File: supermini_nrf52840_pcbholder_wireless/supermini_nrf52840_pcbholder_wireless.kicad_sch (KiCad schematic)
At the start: 14 parts, among them J10 Conn_01x08_Pin, J11 Conn_01x08_Pin, J12 Conn_01x08_Pin, J5 Conn_01x02_Pin, J6 Conn_01x02_Pin, J7 Conn_01x04_Pin, J8 Conn_01x04_Pin, J9 Conn_01x08_Pin, SW1 SW_SPDT, SW2 SW_SPST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

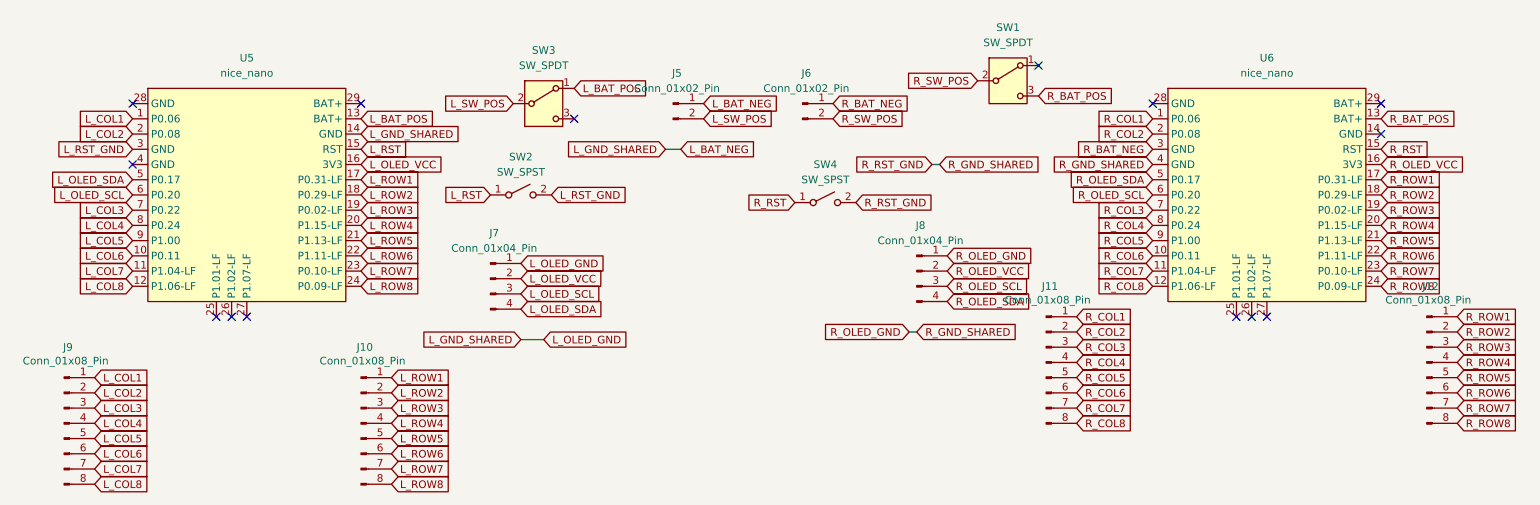
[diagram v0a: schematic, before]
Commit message: change power switch footprint and supermini board placement
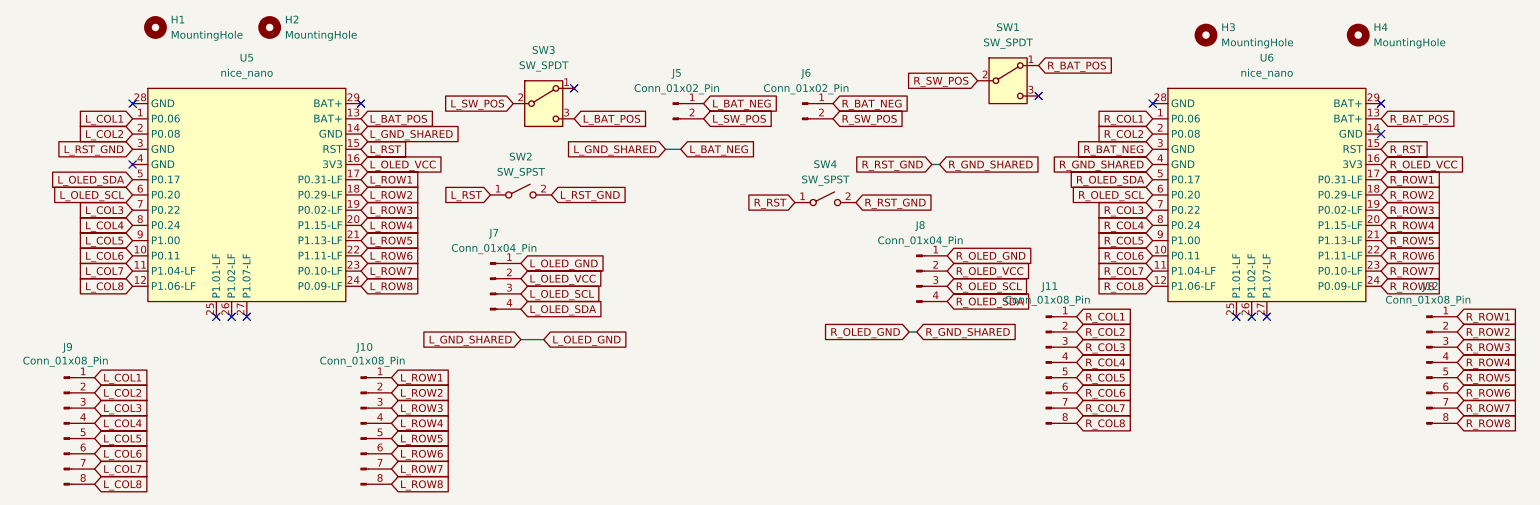
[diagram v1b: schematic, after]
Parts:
- added H1, H2, H3, H4: MountingHole, #footprint:M1.4_tapping_Hole_rev2, symbol Mechanical:MountingHole
- SW1, SW3: footprint #footprint:TGSW_MSK-12D19 -> SLW_864574_5A_RA_N_D:SW_SLW-864574-5A-RA-N-D
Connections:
- net L_BAT_POS: now also SW3.3 (C); no longer SW3.1 (A)
- net R_BAT_POS: now also SW1.1 (A); no longer SW1.3 (C)
